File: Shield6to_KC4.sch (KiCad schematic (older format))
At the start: 23 parts, among them J1 DB9, P1 CONN_8, P2 CONN_8, P3 CONN_9, P4 CONN_9, P5 CONN_8, P6 CONN_8, P7 CONN_8, P8 CONN_8, U1 ID-12LA, U2 MAX232

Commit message: Committer: Esteban Lemos <esteban@mobile.lemos>
 On branch master
 Your branch is up-to-date with 'origin/master'.

 Changes to be committed:
	modified:   Shield6to-cache.lib
	modified:   Shield6to-rescue.lib
	modified:   Shield6to.bak
	deleted:    Shield6to.kicad_pcb
	modified:   Shield6to.kicad_pcb_sin_micro_1.pro
	modified:   Shield6to.pro
	modified:   Shield6to.sch
	new file:   Shield6to_KC4-cache.lib
	new file:   Shield6to_KC4.bak
	new file:   Shield6to_KC4.kicad_pcb
	renamed:    Shield6to.kicad_pcb_sin_micro_1.kicad_pcb -> Shield6to_KC4.kicad_pcb-bak
	new file:   Shield6to_KC4.net
	new file:   Shield6to_KC4.pro
	new file:   Shield6to_KC4.sch
	renamed:    Shield6to+nada.net -> Shield6to_KICAD4.net
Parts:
- C1, C2, C3, C4, C5: footprint Capacitors_ThroughHole:C_Radial_D5_L11_P2 -> Capacitors_ThroughHole:C_Radial_D5_L6_P2.5
- DS1: footprint WC1602A -> Display:RC1602A
- J1: footprint Connect:DB9MC -> Connect:DB9FC
- P1, P2, P5, P6, P7, P8: footprint Pin_Headers:Pin_Header_Straight_1x08 -> Socket_Strips:Socket_Strip_Straight_1x08
- P3, P4: footprint Pin_Headers:Pin_Header_Straight_1x09 -> Socket_Strips:Socket_Strip_Straight_1x09
- RV1, RV2, RV3: footprint Potentiometers:Potentiometer_Bourns_3006Y_Angular_ScrewFront -> Potentiometers:Potentiometer_Bourns_3005_Angular_ScrewFront
- U***1: footprint Housings_DIP:DIP-40_W15.24mm_LongPads -> Housings_DIP:DIP-40_W25.4mm_LongPads
- U2: footprint Housings_DIP:DIP-16_W7.62mm_LongPads -> Housings_DIP:DIP-14_W7.62mm_LongPads
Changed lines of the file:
@@
 EESchema Schematic File Version 2
-LIBS:Shield6to-rescue
 LIBS:power
 LIBS:device
@@
 LIBS:contrib
 LIBS:valves
-LIBS:18f4550
-LIBS:pic18f4550_tqfp
-LIBS:EEST1
-LIBS:Shield6to-cache
+LIBS:Shield6to_KC4-cache
 EELAYER 25 0
 EELAYER END
@@
 F 0 "DS1" H 7450 4400 40  0000 C CNN
 F 1 "LCD16X2" H 8950 4400 40  0000 C CNN
-F 2 "WC1602A" H 8250 3950 35  0000 C CIN
+F 2 "Display:RC1602A" H 8250 3950 35  0001 C CIN
 F 3 "~" H 8250 4000 60  0000 C CNN
 	1    8250 4000
@@
 F 0 "J1" H 10550 3050 70  0000 C CNN
 F 1 "DB9" H 10550 1950 70  0000 C CNN
-F 2 "Connect:DB9MC" H 10550 2500 60  0001 C CNN
+F 2 "Connect:DB9FC" H 10550 2500 60  0001 C CNN
 F 3 "" H 10550 2500 60  0000 C CNN
 	1    10550 2500
@@
 F 0 "C1" H 7600 1500 40  0000 L CNN
 F 1 "1uF" H 7600 1300 40  0000 L CNN
-F 2 "Capacitors_ThroughHole:C_Radial_D5_L11_P2" H 7650 1250 30  0000 C CNN
+F 2 "Capacitors_ThroughHole:C_Radial_D5_L6_P2.5" H 7650 1250 30  0000 C CNN
 F 3 "~" H 7550 1400 300 0000 C CNN
 	1    7550 1400
@@
 F 0 "C4" H 7600 2000 40  0000 L CNN
 F 1 "1uF" H 7600 1800 40  0000 L CNN
-F 2 "Capacitors_ThroughHole:C_Radial_D5_L11_P2" H 7650 1750 30  0000 C CNN
+F 2 "Capacitors_ThroughHole:C_Radial_D5_L6_P2.5" H 7650 1750 30  0000 C CNN
 F 3 "~" H 7550 1900 300 0000 C CNN
 	1    7550 1900
@@
 F 0 "C2" H 9700 1500 40  0000 L CNN
 F 1 "1uF" H 9700 1300 40  0000 L CNN
-F 2 "Capacitors_ThroughHole:C_Radial_D5_L11_P2" H 9750 1250 30  0000 C CNN
+F 2 "Capacitors_ThroughHole:C_Radial_D5_L6_P2.5" H 9750 1250 30  0000 C CNN
 F 3 "~" H 9650 1400 300 0000 C CNN
 	1    9650 1400
@@
 F 0 "C5" H 9700 2100 40  0000 L CNN
 F 1 "1uF" H 9700 1900 40  0000 L CNN
-F 2 "Capacitors_ThroughHole:C_Radial_D5_L11_P2" H 9750 1850 30  0000 C CNN
+F 2 "Capacitors_ThroughHole:C_Radial_D5_L6_P2.5" H 9750 1850 30  0000 C CNN
 F 3 "~" H 9650 2000 300 0000 C CNN
 	1    9650 2000
@@
 F 0 "C3" H 10200 1500 40  0000 L CNN
 F 1 "10uF" H 10200 1300 40  0000 L CNN
-F 2 "Capacitors_ThroughHole:C_Radial_D5_L11_P2" H 10250 1250 30  0000 C CNN
+F 2 "Capacitors_ThroughHole:C_Radial_D5_L6_P2.5" H 10250 1250 30  0000 C CNN
 F 3 "~" H 10150 1400 300 0000 C CNN
 	1    10150 1400
@@
 F 0 "RV1" H 2850 1250 50  0000 C CNN
 F 1 "10K" H 2850 1350 50  0000 C CNN
-F 2 "Potentiometers:Potentiometer_Bourns_3006Y_Angular_ScrewFront" H 2850 1350 60  0001 C CNN
+F 2 "Potentiometers:Potentiometer_Bourns_3005_Angular_ScrewFront" H 2850 1350 60  0001 C CNN
 F 3 "~" H 2850 1350 60  0000 C CNN
 	1    2850 1350
@@
 F 0 "RV3" H 6950 4650 50  0000 C CNN
 F 1 "10K" H 6950 4750 50  0000 C CNN
-F 2 "Potentiometers:Potentiometer_Bourns_3006Y_Angular_ScrewFront" H 6950 4750 60  0001 C CNN
+F 2 "Potentiometers:Potentiometer_Bourns_3005_Angular_ScrewFront" H 6950 4750 60  0001 C CNN
 F 3 "~" H 6950 4750 60  0000 C CNN
 	1    6950 4750
@@
 F 0 "U***1" H 4600 5000 70  0000 C CNN
 F 1 "PIC18F4550" H 4600 4800 70  0000 C CNN
-F 2 "Housings_DIP:DIP-40_W15.24mm_LongPads" H 4600 4900 60  0001 C CNN
+F 2 "Housings_DIP:DIP-40_W25.4mm_LongPads" H 4600 4900 60  0001 C CNN
 F 3 "" H 4600 4900 60  0000 C CNN
 	1    4600 4900
@@
 F 0 "JP1" H 2850 1950 60  0000 C CNN
 F 1 "JUMPER" H 2850 1720 40  0000 C CNN
-F 2 "Pin_Headers:Pin_Header_Straight_1x02" H 2850 1800 60  0000 C CNN
+F 2 "Pin_Headers:Pin_Header_Straight_1x02" H 2850 1800 60  0001 C CNN
 F 3 "~" H 2850 1800 60  0000 C CNN
 	1    2850 1800
@@
 F 0 "RV2" H 3600 1250 50  0000 C CNN
 F 1 "10K" H 3600 1350 50  0000 C CNN
-F 2 "Potentiometers:Potentiometer_Bourns_3006Y_Angular_ScrewFront" H 3600 1350 60  0001 C CNN
+F 2 "Potentiometers:Potentiometer_Bourns_3005_Angular_ScrewFront" H 3600 1350 60  0001 C CNN
 F 3 "~" H 3600 1350 60  0000 C CNN
 	1    3600 1350
@@
 F 0 "JP2" H 3600 1950 60  0000 C CNN
 F 1 "JUMPER" H 3600 1720 40  0000 C CNN
-F 2 "Pin_Headers:Pin_Header_Straight_1x02" H 3600 1800 60  0000 C CNN
+F 2 "Pin_Headers:Pin_Header_Straight_1x02" H 3600 1800 60  0001 C CNN
 F 3 "~" H 3600 1800 60  0000 C CNN
 	1    3600 1800
@@
 F 0 "P1" V 5950 3900 60  0000 C CNN
 F 1 "CONN_8" V 6050 3900 60  0000 C CNN
-F 2 "Pin_Headers:Pin_Header_Straight_1x08" H 6000 3900 60  0001 C CNN
+F 2 "Socket_Strips:Socket_Strip_Straight_1x08" H 6000 3900 60  0001 C CNN
 F 3 "" H 6000 3900 60  0000 C CNN
 	1    6000 3900
@@
 F 0 "P4" V 2600 4050 60  0000 C CNN
 F 1 "CONN_9" V 2700 4050 60  0000 C CNN
-F 2 "Pin_Headers:Pin_Header_Straight_1x09" H 2650 4050 60  0001 C CNN
+F 2 "Socket_Strips:Socket_Strip_Straight_1x09" H 2650 4050 60  0001 C CNN
 F 3 "" H 2650 4050 60  0000 C CNN
 	1    2650 4050
@@
 F 0 "P7" V 9900 5500 60  0000 C CNN
 F 1 "CONN_8" V 10000 5500 60  0000 C CNN
-F 2 "Pin_Headers:Pin_Header_Straight_1x08" H 9950 5500 60  0001 C CNN
+F 2 "Socket_Strips:Socket_Strip_Straight_1x08" H 9950 5500 60  0001 C CNN
 F 3 "" H 9950 5500 60  0000 C CNN
 	1    9950 5500
@@
 F 0 "P3" V 1900 4050 60  0000 C CNN
 F 1 "CONN_9" V 2000 4050 60  0000 C CNN
-F 2 "Pin_Headers:Pin_Header_Straight_1x09" H 1950 4050 60  0001 C CNN
+F 2 "Socket_Strips:Socket_Strip_Straight_1x09" H 1950 4050 60  0001 C CNN
 F 3 "" H 1950 4050 60  0000 C CNN
 	1    1950 4050
@@
 F 0 "P2" V 6550 3900 60  0000 C CNN
 F 1 "CONN_8" V 6650 3900 60  0000 C CNN
-F 2 "Pin_Headers:Pin_Header_Straight_1x08" H 6600 3900 60  0001 C CNN
+F 2 "Socket_Strips:Socket_Strip_Straight_1x08" H 6600 3900 60  0001 C CNN
 F 3 "" H 6600 3900 60  0000 C CNN
 	1    6600 3900
@@
 F 0 "P8" V 10500 5500 60  0000 C CNN
 F 1 "CONN_8" V 10600 5500 60  0000 C CNN
-F 2 "Pin_Headers:Pin_Header_Straight_1x08" H 10550 5500 60  0001 C CNN
+F 2 "Socket_Strips:Socket_Strip_Straight_1x08" H 10550 5500 60  0001 C CNN
 F 3 "" H 10550 5500 60  0000 C CNN
 	1    10550 5500
@@
 F 0 "P6" V 2600 5100 60  0000 C CNN
 F 1 "CONN_8" V 2700 5100 60  0000 C CNN
-F 2 "Pin_Headers:Pin_Header_Straight_1x08" H 2650 5100 60  0001 C CNN
+F 2 "Socket_Strips:Socket_Strip_Straight_1x08" H 2650 5100 60  0001 C CNN
 F 3 "" H 2650 5100 60  0000 C CNN
 	1    2650 5100
@@
 F 0 "P5" V 1900 5100 60  0000 C CNN
 F 1 "CONN_8" V 2000 5100 60  0000 C CNN
-F 2 "Pin_Headers:Pin_Header_Straight_1x08" H 1950 5100 60  0001 C CNN
+F 2 "Socket_Strips:Socket_Strip_Straight_1x08" H 1950 5100 60  0001 C CNN
 F 3 "" H 1950 5100 60  0000 C CNN
 	1    1950 5100
@@
 F 0 "U2" H 7950 2750 50  0000 L CNN
 F 1 "MAX232" H 8600 2750 50  0000 L CNN
-F 2 "Housings_DIP:DIP-16_W7.62mm_LongPads" H 8400 1900 50  0001 C CNN
+F 2 "Housings_DIP:DIP-14_W7.62mm_LongPads" H 8400 1900 50  0001 C CNN
 F 3 "" H 8400 1900 50  0000 C CNN
 	1    8400 1900

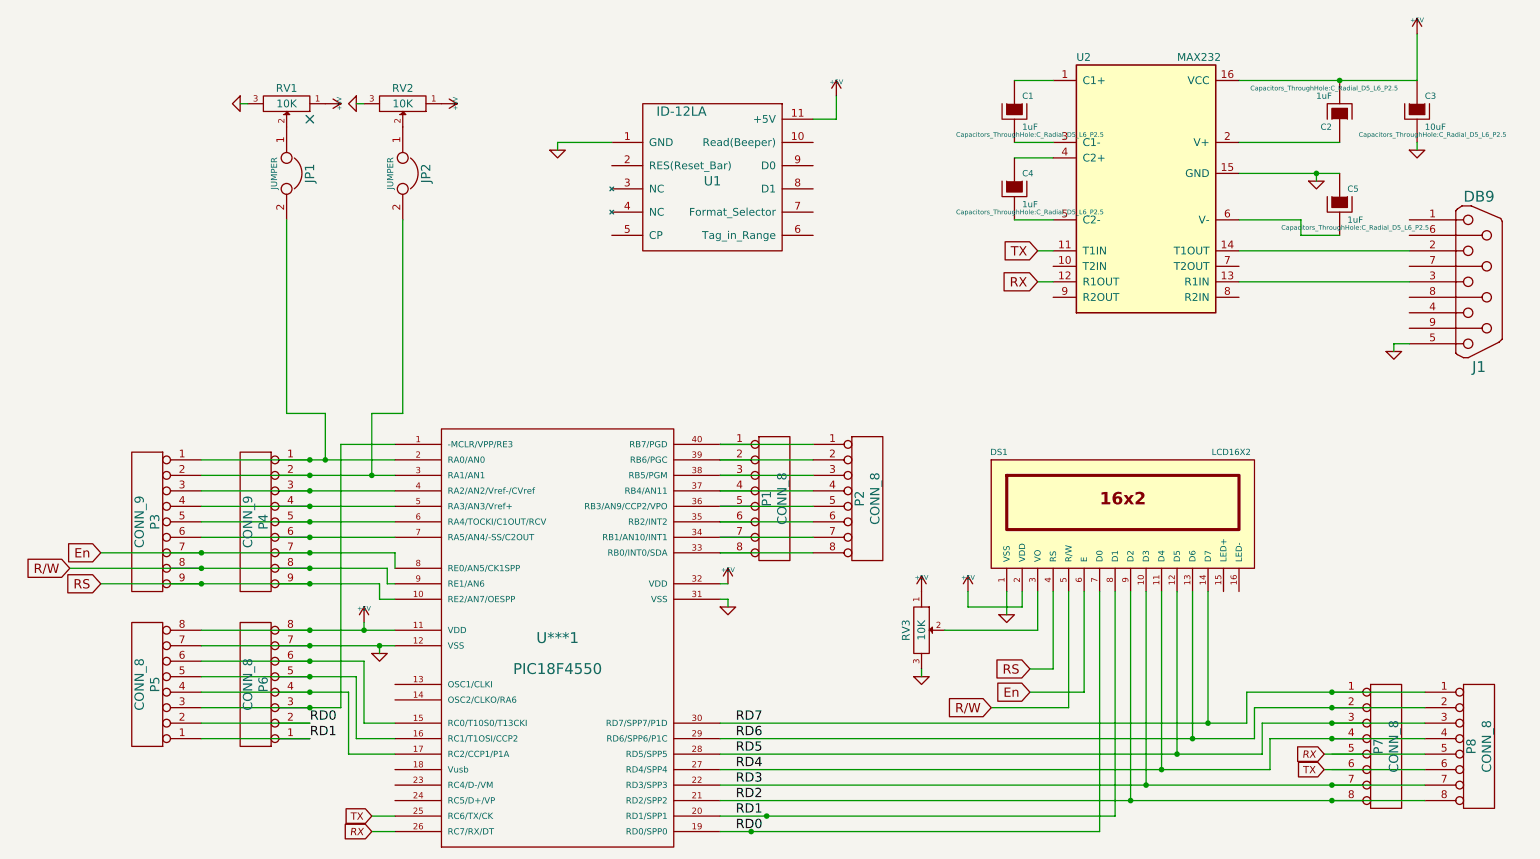
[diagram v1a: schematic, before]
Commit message: Changes to be committed: 	deleted:    Shield6to-cache.lib 	deleted:    Shield6to-rescue.lib 	deleted:    Shield6to.cmp 	deleted:    Shield6to.net 	modified:   Shield6to_KC4-cache.lib 	renamed:    Shield6to.sch -> Shield6to_KC4.bak 	modified:   Shield6to_KC4.kicad_pcb 	modified:   Shield6to_KC4.kicad_pcb-bak 	modified:   Shield6to_KC4.net 	modified:   Shield6to_KC4.sch
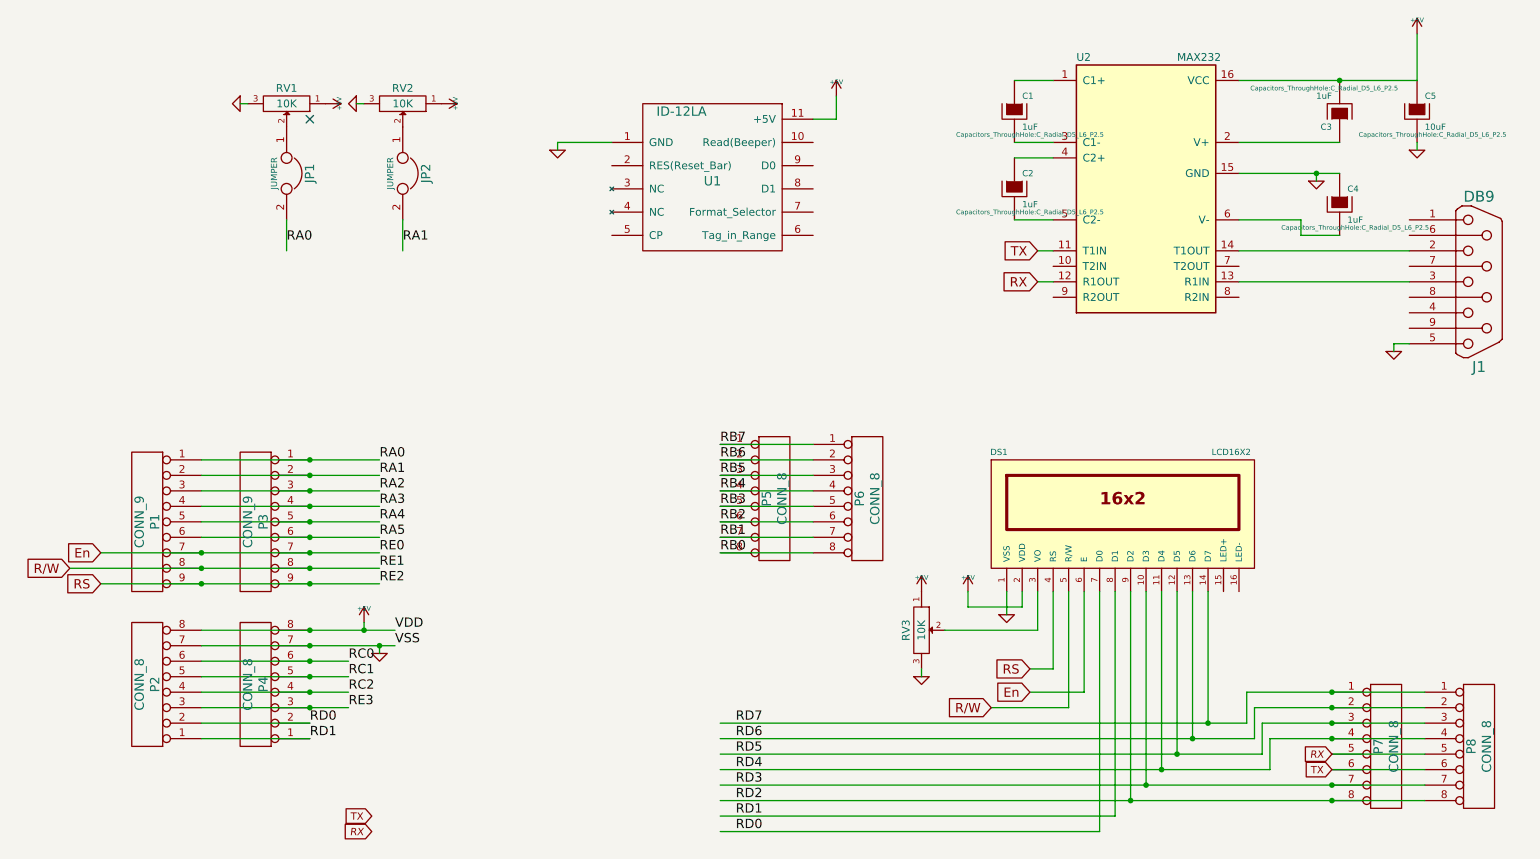
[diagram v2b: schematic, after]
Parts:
- removed U***1: PIC18F4550, Housings_DIP:DIP-40_W25.4mm_LongPads, symbol PIC18F4550
- renumbered C4 to C2, C2 to C3, C5 to C4, C3 to C5, P3 to P1, P5 to P2, P4 to P3, P6 to P4, P1 to P5, P2 to P6
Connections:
- net labels added: RA0, RA1, RA2, RA3, RA4, RA5, RB0, RB1, RB2, RB3, RB4, RB5, RB6, RB7, RC0, RC1, RC2, RE0, RE1, RE2, RE3, VDD, VSS
- wire segments 115 -> 93
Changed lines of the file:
@@
 $EndComp
 $Comp
-L CAPAPOL C4
+L CAPAPOL C2
 U 1 1 56644D07
 P 7550 1900
-F 0 "C4" H 7600 2000 40  0000 L CNN
+F 0 "C2" H 7600 2000 40  0000 L CNN
 F 1 "1uF" H 7600 1800 40  0000 L CNN
 F 2 "Capacitors_ThroughHole:C_Radial_D5_L6_P2.5" H 7650 1750 30  0000 C CNN
@@
 $EndComp
 $Comp
-L CAPAPOL C2
+L CAPAPOL C3
 U 1 1 56644D16
 P 9650 1400
-F 0 "C2" H 9700 1500 40  0000 L CNN
+F 0 "C3" H 9700 1500 40  0000 L CNN
 F 1 "1uF" H 9700 1300 40  0000 L CNN
 F 2 "Capacitors_ThroughHole:C_Radial_D5_L6_P2.5" H 9750 1250 30  0000 C CNN
@@
 $EndComp
 $Comp
-L CAPAPOL C5
+L CAPAPOL C4
 U 1 1 56644D25
 P 9650 2000
-F 0 "C5" H 9700 2100 40  0000 L CNN
+F 0 "C4" H 9700 2100 40  0000 L CNN
 F 1 "1uF" H 9700 1900 40  0000 L CNN
 F 2 "Capacitors_ThroughHole:C_Radial_D5_L6_P2.5" H 9750 1850 30  0000 C CNN
@@
 $EndComp
 $Comp
-L CAPAPOL C3
+L CAPAPOL C5
 U 1 1 56644D34
 P 10150 1400
-F 0 "C3" H 10200 1500 40  0000 L CNN
+F 0 "C5" H 10200 1500 40  0000 L CNN
 F 1 "10uF" H 10200 1300 40  0000 L CNN
 F 2 "Capacitors_ThroughHole:C_Radial_D5_L6_P2.5" H 10250 1250 30  0000 C CNN
@@
 $EndComp
 $Comp
-L PIC18F4550 U***1
-U 1 1 56645347
-P 4600 4900
-F 0 "U***1" H 4600 5000 70  0000 C CNN
-F 1 "PIC18F4550" H 4600 4800 70  0000 C CNN
-F 2 "Housings_DIP:DIP-40_W25.4mm_LongPads" H 4600 4900 60  0001 C CNN
-F 3 "" H 4600 4900 60  0000 C CNN
-	1    4600 4900
-	1    0    0    -1
-$EndComp
-$Comp
 L +5V #PWR09
 U 1 1 56645537
@@
 $Comp
 L GND-RESCUE-Shield6to #PWR011
-U 1 1 56645598
-P 5700 4600
-F 0 "#PWR011" H 5700 4600 30  0001 C CNN
-F 1 "GND" H 5700 4530 30  0001 C CNN
-F 2 "" H 5700 4600 60  0000 C CNN
-F 3 "" H 5700 4600 60  0000 C CNN
-	1    5700 4600
-	1    0    0    -1
-$EndComp
-$Comp
-L +5V #PWR012
-U 1 1 5664559E
-P 5700 4450
-F 0 "#PWR012" H 5700 4540 20  0001 C CNN
-F 1 "+5V" H 5700 4540 30  0000 C CNN
-F 2 "" H 5700 4450 60  0000 C CNN
-F 3 "" H 5700 4450 60  0000 C CNN
-	1    5700 4450
-	1    0    0    -1
-$EndComp
-$Comp
-L GND-RESCUE-Shield6to #PWR013
 U 1 1 566455A4
 P 3450 4900
-F 0 "#PWR013" H 3450 4900 30  0001 C CNN
+F 0 "#PWR011" H 3450 4900 30  0001 C CNN
 F 1 "GND" H 3450 4830 30  0001 C CNN
 F 2 "" H 3450 4900 60  0000 C CNN
@@
 $EndComp
 $Comp
-L +5V #PWR014
+L +5V #PWR012
 U 1 1 56645796
 P 3850 1350
-F 0 "#PWR014" H 3850 1440 20  0001 C CNN
+F 0 "#PWR012" H 3850 1440 20  0001 C CNN
 F 1 "+5V" H 3850 1440 30  0000 C CNN
 F 2 "" H 3850 1350 60  0000 C CNN
@@
 $EndComp
 $Comp
-L GND-RESCUE-Shield6to #PWR015
+L GND-RESCUE-Shield6to #PWR013
 U 1 1 5664579C
 P 3300 1350
-F 0 "#PWR015" H 3300 1350 30  0001 C CNN
+F 0 "#PWR013" H 3300 1350 30  0001 C CNN
 F 1 "GND" H 3300 1280 30  0001 C CNN
 F 2 "" H 3300 1350 60  0000 C CNN
@@
 RX
 $Comp
-L CONN_8 P1
+L CONN_8 P5
 U 1 1 56645AF8
 P 6000 3900
-F 0 "P1" V 5950 3900 60  0000 C CNN
+F 0 "P5" V 5950 3900 60  0000 C CNN
 F 1 "CONN_8" V 6050 3900 60  0000 C CNN
 F 2 "Socket_Strips:Socket_Strip_Straight_1x08" H 6000 3900 60  0001 C CNN
@@
 $EndComp
 $Comp
-L CONN_9 P4
+L CONN_9 P3
 U 1 1 56647247
 P 2650 4050
-F 0 "P4" V 2600 4050 60  0000 C CNN
+F 0 "P3" V 2600 4050 60  0000 C CNN
 F 1 "CONN_9" V 2700 4050 60  0000 C CNN
 F 2 "Socket_Strips:Socket_Strip_Straight_1x09" H 2650 4050 60  0001 C CNN
@@
 $EndComp
 $Comp
-L CONN_9 P3
+L CONN_9 P1
 U 1 1 566482F7
 P 1950 4050
-F 0 "P3" V 1900 4050 60  0000 C CNN
+F 0 "P1" V 1900 4050 60  0000 C CNN
 F 1 "CONN_9" V 2000 4050 60  0000 C CNN
 F 2 "Socket_Strips:Socket_Strip_Straight_1x09" H 1950 4050 60  0001 C CNN
@@
 $EndComp
 $Comp
-L CONN_8 P2
+L CONN_8 P6
 U 1 1 56648303
 P 6600 3900
-F 0 "P2" V 6550 3900 60  0000 C CNN
+F 0 "P6" V 6550 3900 60  0000 C CNN
 F 1 "CONN_8" V 6650 3900 60  0000 C CNN
 F 2 "Socket_Strips:Socket_Strip_Straight_1x08" H 6600 3900 60  0001 C CNN
@@
 $EndComp
 $Comp
-L CONN_8 P6
+L CONN_8 P4
 U 1 1 56645A10
 P 2650 5100
-F 0 "P6" V 2600 5100 60  0000 C CNN
+F 0 "P4" V 2600 5100 60  0000 C CNN
 F 1 "CONN_8" V 2700 5100 60  0000 C CNN
 F 2 "Socket_Strips:Socket_Strip_Straight_1x08" H 2650 5100 60  0001 C CNN
@@
 $EndComp
 $Comp
-L CONN_8 P5
+L CONN_8 P2
 U 1 1 566482FD
 P 1950 5100
-F 0 "P5" V 1900 5100 60  0000 C CNN
+F 0 "P2" V 1900 5100 60  0000 C CNN
 F 1 "CONN_8" V 2000 5100 60  0000 C CNN
 F 2 "Socket_Strips:Socket_Strip_Straight_1x08" H 1950 5100 60  0001 C CNN
@@
 Connection ~ 3000 4050
 Connection ~ 3000 3950
-Connection ~ 3000 3850
-Connection ~ 3000 3750
-Connection ~ 3000 3650
-Connection ~ 3400 3750
-Wire Wire Line
-	3400 3750 3400 3350
-Wire Wire Line
-	3400 3350 3600 3350
-Wire Wire Line
-	3600 3350 3600 2100
-Connection ~ 3100 3650
-Wire Wire Line
-	3100 3650 3100 3350
-Wire Wire Line
-	3100 3350 2850 3350
-Wire Wire Line
-	2850 3350 2850 2100
+Wire Wire Line
+	3600 2300 3600 2100
+Wire Wire Line
+	2850 2300 2850 2100
 Connection ~ 8800 5350
 Wire Wire Line
@@
 	9200 5450 10200 5450
 Wire Wire Line
-	9550 5550 10200 5550
-Wire Wire Line
-	9550 5650 10200 5650
+	9600 5550 10200 5550
+Wire Wire Line
+	9600 5650 10200 5650
 Connection ~ 8400 5750
 Connection ~ 8300 5850
-Connection ~ 5950 5950
 Wire Wire Line
 	2300 5450 3000 5450
-Connection ~ 5850 6050
 Wire Wire Line
 	2300 5350 3000 5350
 Wire Wire Line
-	2300 5250 3200 5250
-Wire Wire Line
-	3200 5250 3200 3550
-Wire Wire Line
-	3200 3550 3550 3550
+	2300 5250 3250 5250
 Wire Wire Line
 	2300 5150 3250 5150
 Wire Wire Line
-	3250 5150 3250 5550
-Wire Wire Line
-	3250 5550 3550 5550
-Wire Wire Line
-	2300 5050 3300 5050
-Wire Wire Line
-	3300 5050 3300 5450
-Wire Wire Line
-	3300 5450 3550 5450
-Wire Wire Line
-	3350 5350 3550 5350
-Wire Wire Line
-	3350 4950 3350 5350
-Wire Wire Line
-	2300 4950 3350 4950
+	2300 5050 3250 5050
+Wire Wire Line
+	2300 4950 3250 4950
 Connection ~ 3450 4850
 Wire Wire Line
-	3450 4450 3450 4550
-Wire Wire Line
-	3450 4550 3550 4550
-Wire Wire Line
-	3500 4350 3500 4450
-Wire Wire Line
-	3500 4450 3550 4450
-Wire Wire Line
-	3550 4250 3550 4350
-Wire Wire Line
-	1650 4250 3550 4250
-Wire Wire Line
-	2300 4150 3550 4150
-Wire Wire Line
-	2300 4050 3550 4050
-Wire Wire Line
-	2300 3950 3550 3950
-Wire Wire Line
-	2300 3850 3550 3850
-Wire Wire Line
-	2300 3750 3550 3750
-Wire Wire Line
-	2300 3650 3550 3650
-Wire Wire Line
-	3400 6050 3550 6050
-Wire Wire Line
-	3400 5950 3550 5950
+	1650 4250 3450 4250
+Wire Wire Line
+	2300 4150 3450 4150
+Wire Wire Line
+	2300 4050 3450 4050
+Wire Wire Line
+	2300 3950 3450 3950
+Wire Wire Line
+	2300 3850 3450 3850
+Wire Wire Line
+	2300 3750 3450 3750
+Wire Wire Line
+	2300 3650 3450 3650
 Wire Wire Line
 	7700 2300 7800 2300
@@
 Wire Wire Line
 	2300 4850 3550 4850
-Wire Wire Line
-	5700 4550 5700 4600
-Wire Wire Line
-	5650 4550 5700 4550
-Wire Wire Line
-	5650 4450 5700 4450
 Wire Wire Line
 	2600 1350 2550 1350
@@
 	7700 2500 7800 2500
 $Comp
-L +5V #PWR016
+L +5V #PWR014
 U 1 1 5665AD12
 P 3350 4700
-F 0 "#PWR016" H 3350 4790 20  0001 C CNN
+F 0 "#PWR014" H 3350 4790 20  0001 C CNN
 F 1 "+5V" H 3350 4790 30  0000 C CNN
 F 2 "" H 3350 4700 60  0000 C CNN
@@
 	1650 4450 3450 4450
 Wire Wire Line
-	1450 4350 3500 4350
-Text GLabel 9550 5650 0    47   Input ~ 0
+	1450 4350 3450 4350
+Text GLabel 9600 5650 0    47   Input ~ 0
 TX
-Text GLabel 9550 5550 0    47   Input Italic 0
+Text GLabel 9600 5550 0    47   Input Italic 0
 RX
 Text Label 5750 5350 0    60   ~ 0
@@
 $EndComp
 $Comp
-L +5V #PWR017
+L +5V #PWR015
 U 1 1 566A13AF
 P 6400 1300
-F 0 "#PWR017" H 6400 1390 20  0001 C CNN
+F 0 "#PWR015" H 6400 1390 20  0001 C CNN
 F 1 "+5V" H 6400 1390 30  0000 C CNN
 F 2 "" H 6400 1300 60  0000 C CNN
@@
 $EndComp
 $Comp
-L GND-RESCUE-Shield6to #PWR018
+L GND-RESCUE-Shield6to #PWR016
 U 1 1 566A159D
 P 4600 1650
-F 0 "#PWR018" H 4600 1650 30  0001 C CNN
+F 0 "#PWR016" H 4600 1650 30  0001 C CNN
 F 1 "GND" H 4600 1580 30  0001 C CNN
 F 2 "" H 4600 1650 60  0000 C CNN
@@
 Wire Wire Line
 	9000 2100 9400 2100
+Text Label 3450 3650 0    60   ~ 0
+RA0
+Text Label 3450 3750 0    60   ~ 0
+RA1
+Text Label 3450 3850 0    60   ~ 0
+RA2
+Text Label 3450 3950 0    60   ~ 0
+RA3
+Text Label 3450 4050 0    60   ~ 0
+RA4
+Text Label 3450 4150 0    60   ~ 0
+RA5
+Text Label 3450 4250 0    60   ~ 0
+RE0
+Text Label 3450 4350 0    60   ~ 0
+RE1
+Text Label 3450 4450 0    60   ~ 0
+RE2
+Text Label 3250 5250 0    60   ~ 0
+RE3
+Text Label 3600 2250 0    60   ~ 0
+RA1
+Text Label 2850 2250 0    60   ~ 0
+RA0
+Text Label 3250 4950 0    60   ~ 0
+RC0
+Text Label 3250 5050 0    60   ~ 0
+RC1
+Text Label 3250 5150 0    60   ~ 0
+RC2
+Text Label 3550 4750 0    60   ~ 0
+VDD
+Text Label 3550 4850 0    60   ~ 0
+VSS
+Text Label 5650 3550 0    60   ~ 0
+RB7
+Text Label 5650 3650 0    60   ~ 0
+RB6
+Text Label 5650 3750 0    60   ~ 0
+RB5
+Text Label 5650 3850 0    60   ~ 0
+RB4
+Text Label 5650 3950 0    60   ~ 0
+RB3
+Text Label 5650 4050 0    60   ~ 0
+RB2
+Text Label 5650 4150 0    60   ~ 0
+RB1
+Text Label 5650 4250 0    60   ~ 0
+RB0
+Connection ~ 3000 3850
+Connection ~ 3000 3750
+Connection ~ 3000 3650
 $EndSCHEMATC
